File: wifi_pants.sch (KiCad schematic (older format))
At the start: 22 parts, among them P1 CONN_02X20, P2 POWER / UART, P3 JST PH POWER IN, U1 ESP-12E, U2 TPS6123x

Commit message: v3 complete layout
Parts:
- renumbered C4 to C2, C5 to C3, C6 to C4, C2 to C5, C3 to C6
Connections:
- net /PSU_SHDN renamed /SHDN
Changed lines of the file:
@@
 Sheet 1 1
 Title "ESP8266 WiFi Module for Raspberry Pi"
-Date "2016-02-10"
-Rev "v3b0"
+Date "2016-02-14"
+Rev "v3"
 Comp "Andrew Litt"
 Comment1 "https://github.com/al177/wifi_pants"
@@
 NoConn ~ 8700 3750
 Text GLabel 7500 1000 0    39   Output ~ 0
-/PSU_SHDN
+/SHDN
 Text Notes 9100 1200 0    39   ~ 0
 /PSU_SHDN
 Text GLabel 1150 2450 0    39   Input ~ 0
-/PSU_SHDN
+/SHDN
 Text GLabel 7500 1300 0    39   Output ~ 0
 PWR_IN
@@
 $EndComp
 $Comp
-L C C4
+L C C2
 U 1 1 56BBBDB1
 P 5000 2050
-F 0 "C4" H 5025 2150 50  0000 L CNN
+F 0 "C2" H 5025 2150 50  0000 L CNN
 F 1 "10uF X5R" V 5150 1600 50  0000 L CNN
 F 2 "mcous:0805(2012m)-CHIP-CAP" H 5038 1900 50  0001 C CNN
@@
 $EndComp
 $Comp
-L C C5
+L C C3
 U 1 1 56BE3AE2
 P 5300 2050
-F 0 "C5" H 5325 2150 50  0000 L CNN
+F 0 "C3" H 5325 2150 50  0000 L CNN
 F 1 "10uF X5R" V 5450 1600 50  0000 L CNN
 F 2 "mcous:0805(2012m)-CHIP-CAP" H 5338 1900 50  0001 C CNN
@@
 $EndComp
 $Comp
-L C C6
+L C C4
 U 1 1 56BE3B54
 P 5600 2050
-F 0 "C6" H 5625 2150 50  0000 L CNN
+F 0 "C4" H 5625 2150 50  0000 L CNN
 F 1 "10uF X5R" V 5750 1600 50  0000 L CNN
 F 2 "mcous:0805(2012m)-CHIP-CAP" H 5638 1900 50  0001 C CNN
@@
 $EndComp
 $Comp
-L C C3
+L C C6
 U 1 1 56BE4135
 P 1400 1900
-F 0 "C3" H 1425 2000 50  0000 L CNN
+F 0 "C6" H 1425 2000 50  0000 L CNN
 F 1 "22uF X5R" V 1250 1700 50  0000 L CNN
 F 2 "mcous:0805(2012m)-CHIP-CAP" H 1438 1750 50  0001 C CNN
@@
 $EndComp
 $Comp
-L C C2
+L C C5
 U 1 1 56BE46FB
 P 2200 2750
-F 0 "C2" H 2225 2850 50  0000 L CNN
+F 0 "C5" H 2225 2850 50  0000 L CNN
 F 1 "0.15uF X5R" V 2400 2450 50  0000 L CNN
 F 2 "mcous:0603(1608m)-CHIP-CAP" H 2238 2600 50  0001 C CNN

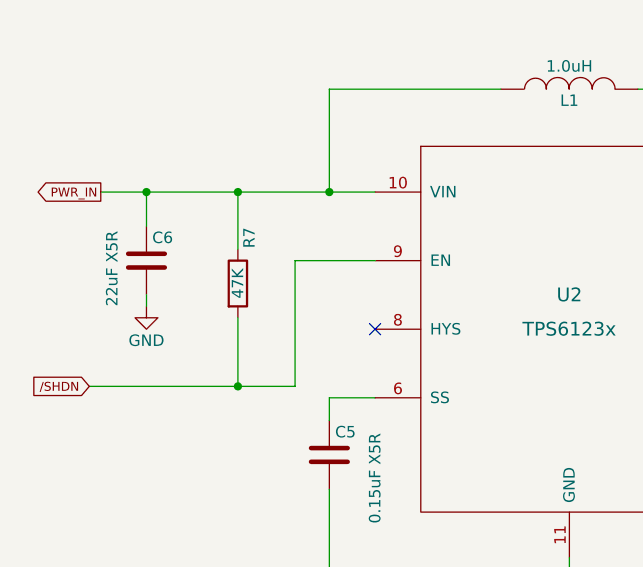
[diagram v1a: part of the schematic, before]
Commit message: Fix some part#s in the schematic, clean up the back side silk for the JST connector
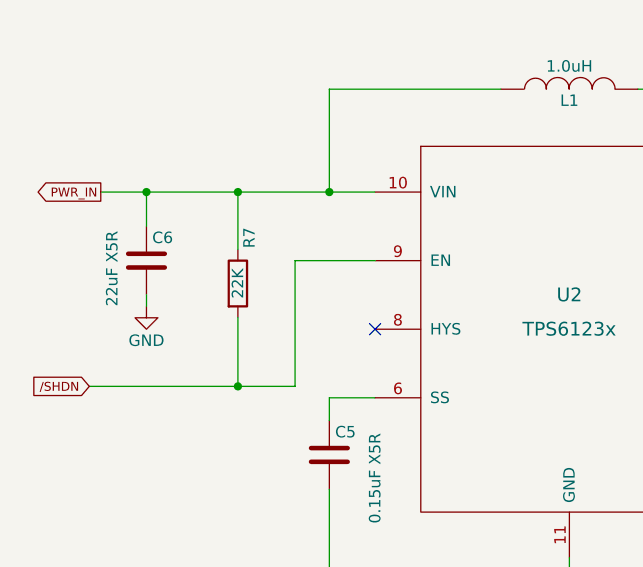
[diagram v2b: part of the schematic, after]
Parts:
- C5: Digikey Link http://www.digikey.com/product-detail/en/GRM155R61A154KE19D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 -> https://www.digikey.com/product-detail/en/GRM188R61A154KA01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; Digikey PN 490-5889-1-ND -> 490-11495-1-ND; MFG Part Num GRM155R61A154KE19D -> GRM188R61A154KA01D
- R7: value 47K -> 22K
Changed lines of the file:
@@
 P 1800 2000
 F 0 "R7" V 1850 2200 50  0000 C CNN
-F 1 "47K" V 1800 2000 50  0000 C CNN
+F 1 "22K" V 1800 2000 50  0000 C CNN
 F 2 "mcous:0603(1608m)-CHIP-RESISTOR" V 1730 2000 50  0001 C CNN
 F 3 "" H 1800 2000 50  0000 C CNN
@@
 F 3 "" H 2200 2750 50  0001 C CNN
 F 4 "Murata" H 2200 2750 60  0001 C CNN "MFG Name"
-F 5 "GRM155R61A154KE19D" H 2200 2750 60  0001 C CNN "MFG Part Num"
-F 6 "490-5889-1-ND" H 2200 2750 60  0001 C CNN "Digikey PN"
-F 7 "http://www.digikey.com/product-detail/en/GRM155R61A154KE19D/490-5889-1-ND/3315236" H 2200 2750 60  0001 C CNN "Digikey Link"
+F 5 "GRM188R61A154KA01D" H 2200 2750 60  0001 C CNN "MFG Part Num"
+F 6 "490-11495-1-ND" H 2200 2750 60  0001 C CNN "Digikey PN"
+F 7 "https://www.digikey.com/product-detail/en/GRM188R61A154KA01D/490-11495-1-ND/5333335" H 2200 2750 60  0001 C CNN "Digikey Link"
 F 8 "NA" H 2200 2750 60  0001 C CNN "2nd Distrib PN"
 F 9 "NA" H 2200 2750 60  0001 C CNN "2nd Distrib Link"

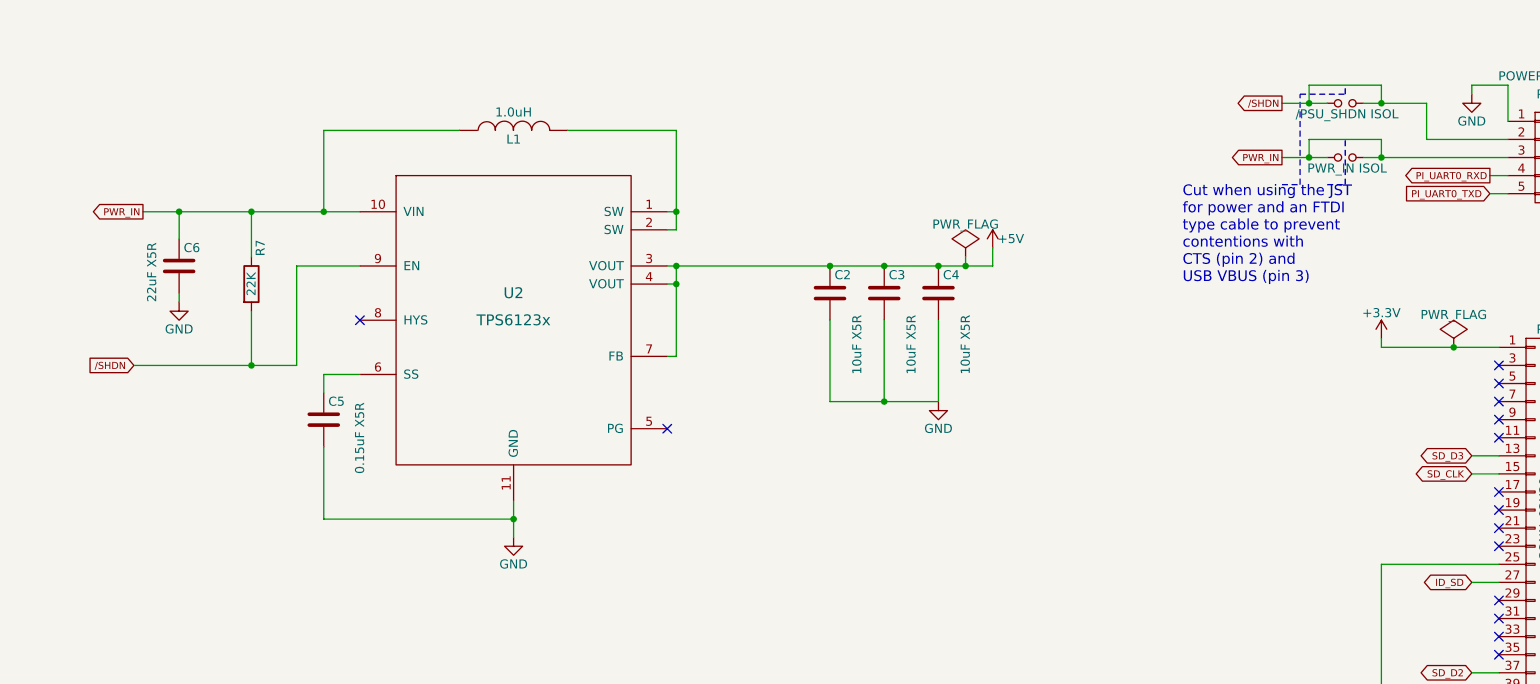
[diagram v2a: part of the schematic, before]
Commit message: Add UVLO for LiPo, rearrange boost layout, make PWR_IN on header disconnected by default
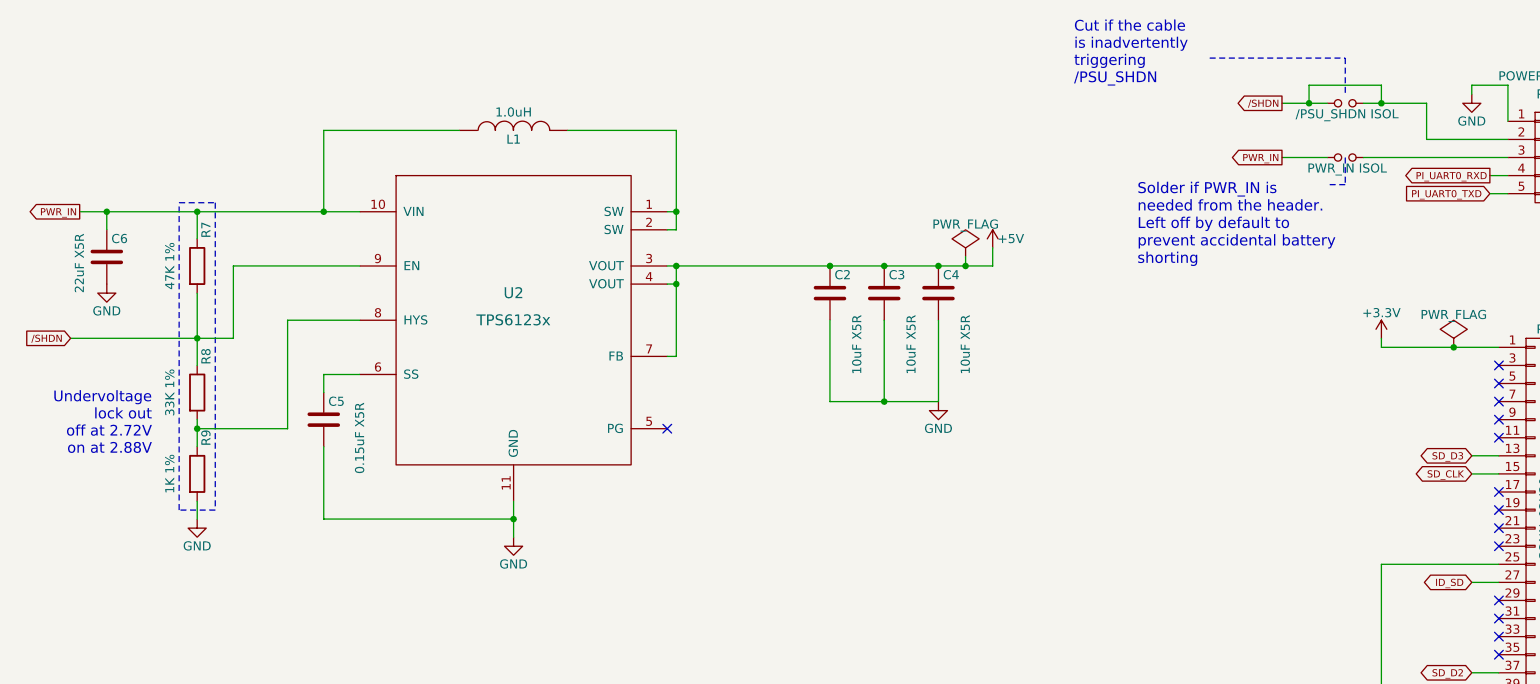
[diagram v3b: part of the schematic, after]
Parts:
- added R8: 33K 1%, mcous:0603(1608m)-CHIP-RESISTOR, symbol R
- added R9: 1K 1%, mcous:0603(1608m)-CHIP-RESISTOR, symbol R
- R7: value 22K -> 47K 1%; Digikey Link http://www.digikey.com/product-detail/en/ERJ-3GEYJ223V/P22K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 -> http://www.digikey.com/product-search/en?keywords=P47.0KHCT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; Digikey PN P22KGCT-ND -> P47.0KHCT-ND; MFG Part Num ERJ-3GEYJ223V -> ERJ-3EKF4702V
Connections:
- net /SHDN: now also R8.1
- net GND: now also R9.2
- net PWR_IN: no longer JP2.2, P2.3 (P3)
- net at U2.8 (HYS): now also R8.2, R9.1
- new net: JP2.2, P2.3 (P3)
- no-connect marks 35 -> 34
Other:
- note added: "Cut if the cable\nis inadvertently\ntriggering\n/PSU_SHDN"
- note added: "Solder if PWR_IN is\nneeded from the header.\nLeft off by default to\nprevent accidental battery\nshorting"
- note added: "Undervoltage\nlock out\noff at 2.72V\non at 2.88V"
- note removed: "Cut when using the JST\nfor power and an FTDI\ntype cable to prevent\ncontentions with\nCTS (pin 2) and\nUSB VBUS (pin 3)"
- moved on the sheet: C6, R7
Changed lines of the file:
@@
 LIBS:contrib
 LIBS:valves
-LIBS:ESP8266
 LIBS:wifi_pants-cache
 EELAYER 25 0
@@
 Sheet 1 1
 Title "ESP8266 WiFi Module for Raspberry Pi"
-Date "2016-02-14"
-Rev "v3"
+Date "2016-03-09"
+Rev "r4"
 Comp "Andrew Litt"
 Comment1 "https://github.com/al177/wifi_pants"
@@
 Text Notes 9100 1200 0    39   ~ 0
 /PSU_SHDN
-Text GLabel 1150 2450 0    39   Input ~ 0
+Text GLabel 800  2300 0    39   Input ~ 0
 /SHDN
 Text GLabel 7500 1300 0    39   Output ~ 0
@@
 Text Notes 9100 1300 0    39   ~ 0
 PWR_IN
-Text GLabel 1200 1600 0    39   Output ~ 0
+Text GLabel 850  1600 0    39   Output ~ 0
 PWR_IN
 $Comp
@@
 L GND #PWR014
 U 1 1 56BC3486
-P 1400 2100
-F 0 "#PWR014" H 1400 1850 50  0001 C CNN
-F 1 "GND" H 1400 1950 50  0000 C CNN
-F 2 "" H 1400 2100 50  0000 C CNN
-F 3 "" H 1400 2100 50  0000 C CNN
-	1    1400 2100
+P 1000 2000
+F 0 "#PWR014" H 1000 1750 50  0001 C CNN
+F 1 "GND" H 1000 1850 50  0000 C CNN
+F 2 "" H 1000 2000 50  0000 C CNN
+F 3 "" H 1000 2000 50  0000 C CNN
+	1    1000 2000
 	1    0    0    -1
 $EndComp
@@
 	1    0    0    -1
 $EndComp
-Text Notes 6950 2000 0    59   ~ 0
-Cut when using the JST\nfor power and an FTDI\ntype cable to prevent\ncontentions with\nCTS (pin 2) and\nUSB VBUS (pin 3)
+Text Notes 6350 900  0    59   ~ 0
+Cut if the cable\nis inadvertently\ntriggering\n/PSU_SHDN
 $Comp
 L R R7
 U 1 1 56BB8C7C
-P 1800 2000
-F 0 "R7" V 1850 2200 50  0000 C CNN
-F 1 "22K" V 1800 2000 50  0000 C CNN
-F 2 "mcous:0603(1608m)-CHIP-RESISTOR" V 1730 2000 50  0001 C CNN
-F 3 "" H 1800 2000 50  0000 C CNN
-F 4 "Panasonic Electronic Components" H 1800 2000 60  0001 C CNN "MFG Name"
-F 5 "ERJ-3GEYJ223V" H 1800 2000 60  0001 C CNN "MFG Part Num"
-F 6 "P22KGCT-ND" H 1800 2000 60  0001 C CNN "Digikey PN"
-F 7 "http://www.digikey.com/product-detail/en/ERJ-3GEYJ223V/P22KGCT-ND/134757" H 1800 2000 60  0001 C CNN "Digikey Link"
-F 8 "NA" H 1800 2000 60  0001 C CNN "2nd Distrib PN"
-F 9 "NA" H 1800 2000 60  0001 C CNN "2nd Distrib Link"
-	1    1800 2000
+P 1500 1900
+F 0 "R7" V 1550 2100 50  0000 C CNN
+F 1 "47K 1%" V 1350 1900 50  0000 C CNN
+F 2 "mcous:0603(1608m)-CHIP-RESISTOR" V 1430 1900 50  0001 C CNN
+F 3 "" H 1500 1900 50  0000 C CNN
+F 4 "Panasonic Electronic Components" H 1500 1900 60  0001 C CNN "MFG Name"
+F 5 "ERJ-3EKF4702V" H 1500 1900 60  0001 C CNN "MFG Part Num"
+F 6 "P47.0KHCT-ND" H 1500 1900 60  0001 C CNN "Digikey PN"
+F 7 "http://www.digikey.com/product-search/en?keywords=P47.0KHCT-ND" H 1500 1900 60  0001 C CNN "Digikey Link"
+F 8 "NA" H 1500 1900 60  0001 C CNN "2nd Distrib PN"
+F 9 "NA" H 1500 1900 60  0001 C CNN "2nd Distrib Link"
+	1    1500 1900
 	1    0    0    -1
 $EndComp
@@
 L C C6
 U 1 1 56BE4135
-P 1400 1900
-F 0 "C6" H 1425 2000 50  0000 L CNN
-F 1 "22uF X5R" V 1250 1700 50  0000 L CNN
-F 2 "mcous:0805(2012m)-CHIP-CAP" H 1438 1750 50  0001 C CNN
-F 3 "http://ds.yuden.co.jp/TYCOMPAS/ut/detail.do?productNo=LMK316BJ106KL-T&fileName=LMK316BJ106KL-T_SS&mode=specSheetDownload" H 1400 1900 50  0001 C CNN
-F 4 "Taiyo Yuden" H 1400 1900 60  0001 C CNN "MFG Name"
-F 5 "LMK212BJ226MG-T" H 1400 1900 60  0001 C CNN "MFG Part Num"
-F 6 "587-1958-1-ND" H 1400 1900 60  0001 C CNN "Digikey PN"
-F 7 "http://www.digikey.com/product-detail/en/LMK212BJ226MG-T/587-1958-1-ND/1646621" H 1400 1900 60  0001 C CNN "Digikey Link"
-F 8 "NA" H 1400 1900 60  0001 C CNN "2nd Distrib PN"
-F 9 "NA" H 1400 1900 60  0001 C CNN "2nd Distrib Link"
-	1    1400 1900
+P 1000 1850
+F 0 "C6" H 1025 1950 50  0000 L CNN
+F 1 "22uF X5R" V 850 1650 50  0000 L CNN
+F 2 "mcous:0805(2012m)-CHIP-CAP" H 1038 1700 50  0001 C CNN
+F 3 "http://ds.yuden.co.jp/TYCOMPAS/ut/detail.do?productNo=LMK316BJ106KL-T&fileName=LMK316BJ106KL-T_SS&mode=specSheetDownload" H 1000 1850 50  0001 C CNN
+F 4 "Taiyo Yuden" H 1000 1850 60  0001 C CNN "MFG Name"
+F 5 "LMK212BJ226MG-T" H 1000 1850 60  0001 C CNN "MFG Part Num"
+F 6 "587-1958-1-ND" H 1000 1850 60  0001 C CNN "Digikey PN"
+F 7 "http://www.digikey.com/product-detail/en/LMK212BJ226MG-T/587-1958-1-ND/1646621" H 1000 1850 60  0001 C CNN "Digikey Link"
+F 8 "NA" H 1000 1850 60  0001 C CNN "2nd Distrib PN"
+F 9 "NA" H 1000 1850 60  0001 C CNN "2nd Distrib Link"
+	1    1000 1850
 	1    0    0    -1
 $EndComp
@@
 	1    0    0    -1
 $EndComp
-NoConn ~ 2400 2200
 NoConn ~ 4100 2800
 $Comp
@@
 	8550 900  8550 950
 Wire Wire Line
-	7950 1300 8750 1300
-Wire Wire Line
 	8650 1400 8750 1400
 Wire Wire Line
@@
 	8300 1200 8750 1200
 Wire Wire Line
-	7500 1300 7750 1300
-Wire Wire Line
 	7650 1000 7650 900
 Wire Wire Line
@@
 Wire Wire Line
 	8050 900  8050 1000
-Wire Wire Line
-	8050 1300 8050 1200
-Wire Wire Line
-	8050 1200 7650 1200
-Wire Wire Line
-	7650 1200 7650 1300
 Connection ~ 7650 1000
 Connection ~ 8050 1000
-Connection ~ 8050 1300
-Connection ~ 7650 1300
-Wire Notes Line
-	7750 1450 7850 1450
-Wire Notes Line
-	7600 1450 7600 950
-Wire Notes Line
-	7600 950  7850 950
-Wire Notes Line
-	7850 950  7850 900
-Wire Notes Line
-	7850 1450 7850 1200
-Wire Notes Line
-	7500 1450 7600 1450
-Wire Wire Line
-	1200 1600 2400 1600
+Wire Notes Line
+	7850 1450 7750 1450
+Wire Wire Line
+	850  1600 2400 1600
 Wire Wire Line
 	2950 1150 2200 1150
@@
 	4150 2400 4100 2400
 Connection ~ 4150 2000
-Wire Wire Line
-	1150 2450 2050 2450
-Wire Wire Line
-	2050 2450 2050 1900
-Wire Wire Line
-	2050 1900 2400 1900
-Connection ~ 1400 1600
-Wire Wire Line
-	1400 1750 1400 1600
-Wire Wire Line
-	1400 2050 1400 2100
-Wire Wire Line
-	1800 2450 1800 2150
-Connection ~ 1800 2450
-Wire Wire Line
-	1800 1850 1800 1600
-Connection ~ 1800 1600
 Wire Wire Line
 	5000 2200 5000 2650
@@
 	1    0    0    -1
 $EndComp
+Wire Wire Line
+	1000 1700 1000 1600
+Connection ~ 1000 1600
+$Comp
+L R R8
+U 1 1 56D0992F
+P 1500 2600
+F 0 "R8" V 1550 2800 50  0000 C CNN
+F 1 "33K 1%" V 1350 2600 50  0000 C CNN
+F 2 "mcous:0603(1608m)-CHIP-RESISTOR" V 1430 2600 50  0001 C CNN
+F 3 "" H 1500 2600 50  0000 C CNN
+F 4 "Panasonic Electronic Components" H 1500 2600 60  0001 C CNN "MFG Name"
+F 5 "ERJ-3EKF3302V" H 1500 2600 60  0001 C CNN "MFG Part Num"
+F 6 "P33.0KHCT-ND" H 1500 2600 60  0001 C CNN "Digikey PN"
+F 7 "http://www.digikey.com/product-search/en?keywords=P33.0KHCT-ND" H 1500 2600 60  0001 C CNN "Digikey Link"
+F 8 "NA" H 1500 2600 60  0001 C CNN "2nd Distrib PN"
+F 9 "NA" H 1500 2600 60  0001 C CNN "2nd Distrib Link"
+	1    1500 2600
+	1    0    0    -1
+$EndComp
+$Comp
+L R R9
+U 1 1 56D099AE
+P 1500 3050
+F 0 "R9" V 1550 3250 50  0000 C CNN
+F 1 "1K 1%" V 1350 3050 50  0000 C CNN
+F 2 "mcous:0603(1608m)-CHIP-RESISTOR" V 1430 3050 50  0001 C CNN
+F 3 "" H 1500 3050 50  0000 C CNN
+F 4 "Panasonic Electronic Components" H 1500 3050 60  0001 C CNN "MFG Name"
+F 5 "ERJ-3EKF1001V" H 1500 3050 60  0001 C CNN "MFG Part Num"
+F 6 "P1.00KHCT-ND" H 1500 3050 60  0001 C CNN "Digikey PN"
+F 7 "http://www.digikey.com/product-detail/en/ERJ-3EKF1001V/P1.00KHCT-ND/198071" H 1500 3050 60  0001 C CNN "Digikey Link"
+F 8 "NA" H 1500 3050 60  0001 C CNN "2nd Distrib PN"
+F 9 "NA" H 1500 3050 60  0001 C CNN "2nd Distrib Link"
+	1    1500 3050
+	1    0    0    -1
+$EndComp
+$Comp
+L GND #PWR019
+U 1 1 56D09A18
+P 1500 3300
+F 0 "#PWR019" H 1500 3050 50  0001 C CNN
+F 1 "GND" H 1500 3150 50  0000 C CNN
+F 2 "" H 1500 3300 50  0000 C CNN
+F 3 "" H 1500 3300 50  0000 C CNN
+	1    1500 3300
+	1    0    0    -1
+$EndComp
+Wire Wire Line
+	2400 2200 2000 2200
+Wire Wire Line
+	2000 2200 2000 2800
+Wire Wire Line
+	2000 2800 1500 2800
+Wire Wire Line
+	1500 2750 1500 2900
+Connection ~ 1500 2800
+Wire Wire Line
+	1500 3200 1500 3300
+Connection ~ 1500 1600
+Wire Wire Line
+	2400 1900 1700 1900
+Wire Wire Line
+	1700 1900 1700 2300
+Wire Wire Line
+	1700 2300 800  2300
+Connection ~ 1500 2300
+Wire Wire Line
+	1500 1750 1500 1600
+Wire Wire Line
+	1500 2050 1500 2450
+Wire Notes Line
+	1400 1550 1600 1550
+Wire Notes Line
+	1600 1550 1600 3250
+Wire Notes Line
+	1600 3250 1400 3250
+Wire Notes Line
+	1400 3250 1400 1550
+Text Notes 1250 2950 2    59   ~ 0
+Undervoltage\nlock out\noff at 2.72V\non at 2.88V
+Wire Wire Line
+	7950 1300 8750 1300
+Wire Wire Line
+	7500 1300 7750 1300
+Wire Notes Line
+	7100 750  7850 750
+Wire Notes Line
+	7850 750  7850 950
+Text Notes 6700 1900 0    60   ~ 0
+Solder if PWR_IN is\nneeded from the header.\nLeft off by default to\nprevent accidental battery\nshorting
+Wire Notes Line
+	7850 1300 7850 1450
 $EndSCHEMATC
